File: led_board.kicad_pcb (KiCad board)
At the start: 2 copper layers, 185 x 120 mm, 52 parts, among them J1 Conn_Coaxial, J2 Conn_Coaxial, J3 Conn_Coaxial, J4 Conn_Coaxial, J5 Conn_Coaxial, J6 Conn_Coaxial, J7 Conn_Coaxial, J8 Conn_Coaxial

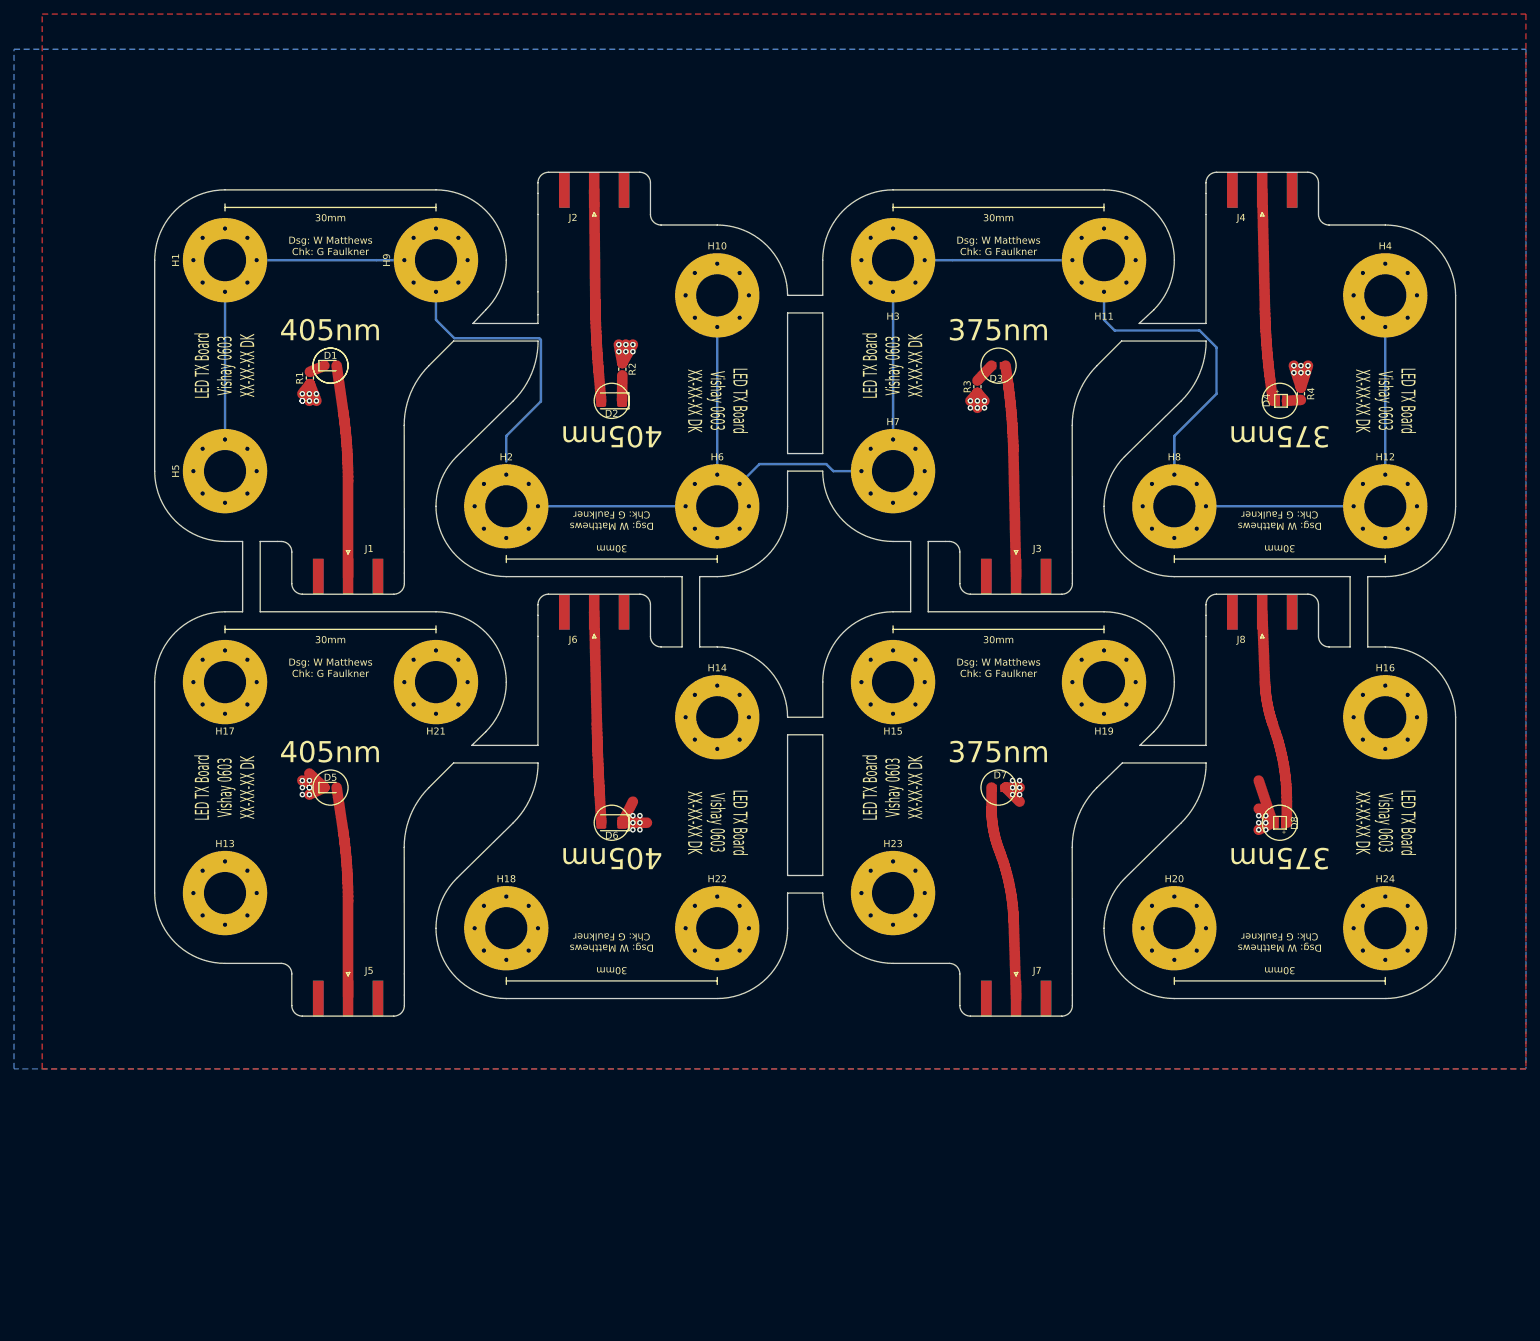
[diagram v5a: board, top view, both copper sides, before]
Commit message: via fencing + mask for all rf traces.
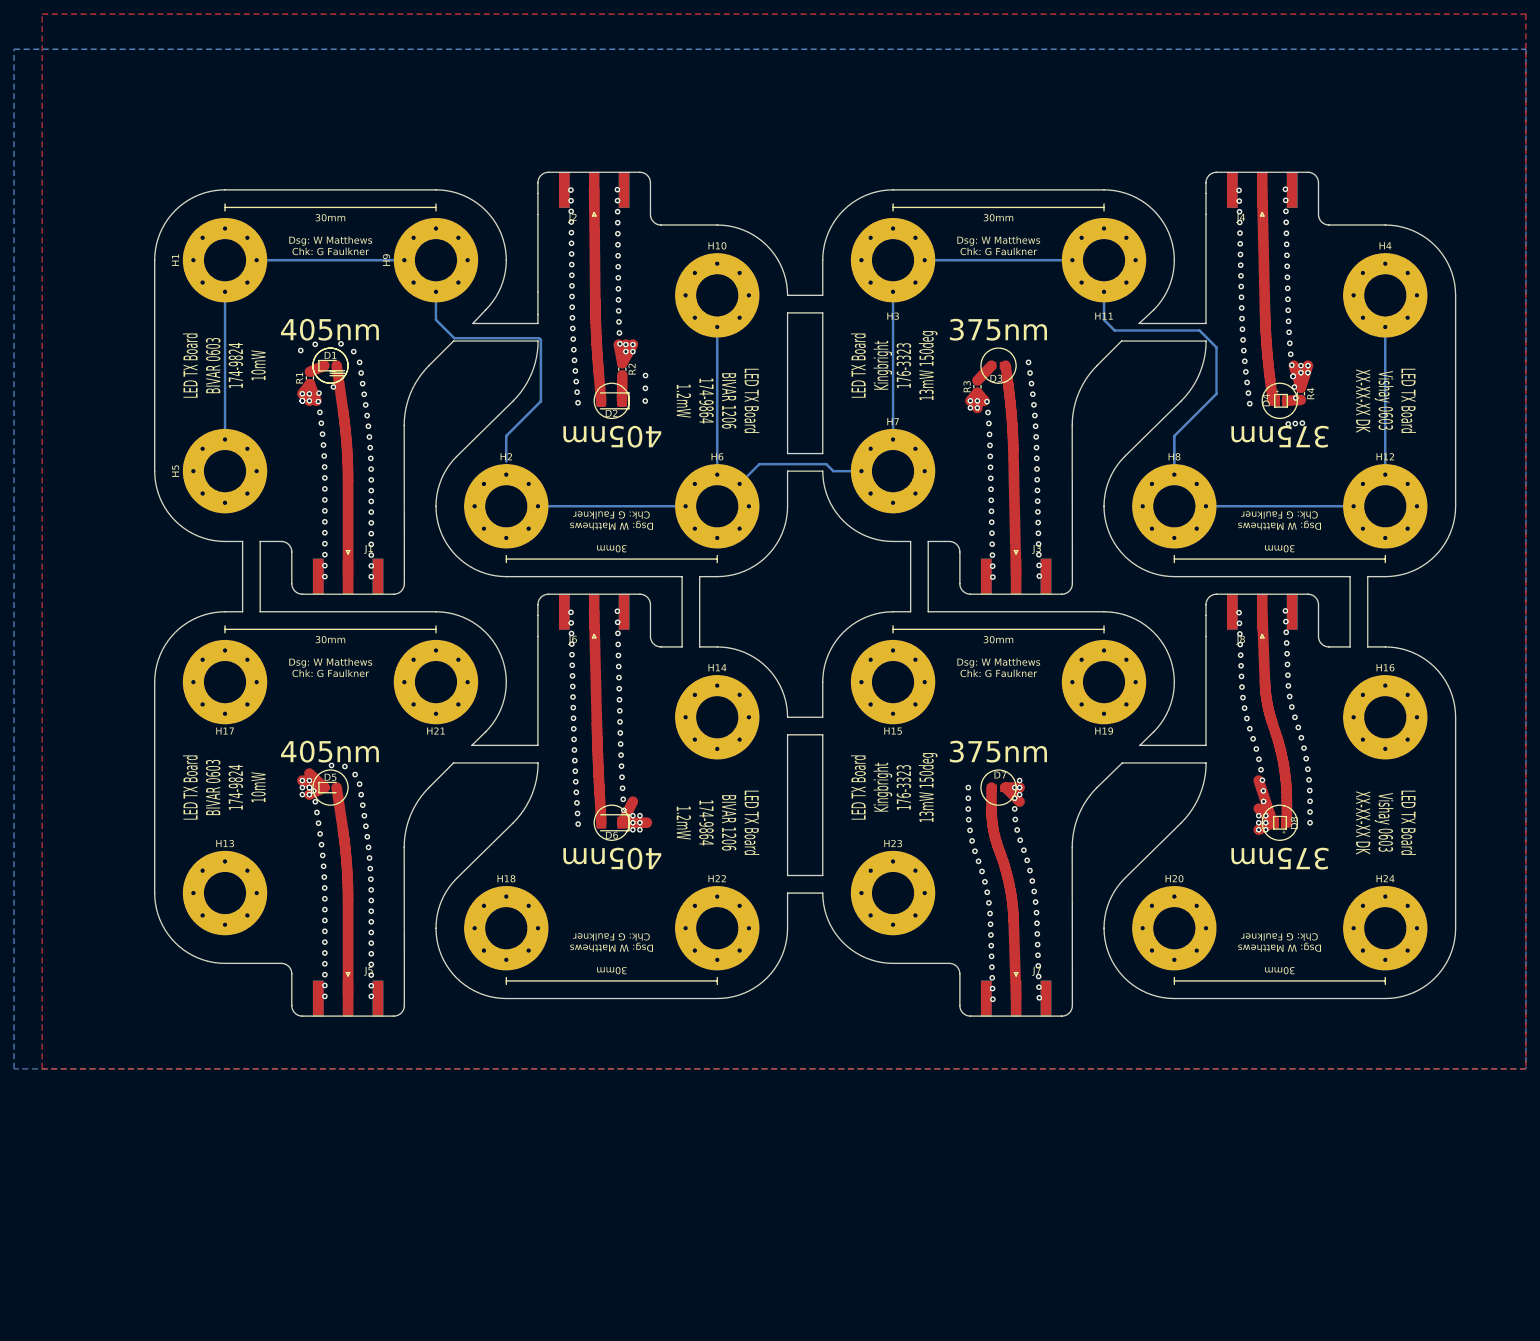
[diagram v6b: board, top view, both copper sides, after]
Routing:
- net Net-(D4-Pad1): vias 0 -> 1
- net GND: vias 51 -> 371
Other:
- board text added: "LED TX Board BIVAR 0603 174-9824 10mW"
- board text added: "LED TX Board BIVAR 1206 174-9864 1.2mW"
- board text added: "LED TX Board Kingbright 176-3323 13mW 150deg"

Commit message: finalised
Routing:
- net GND: track 421.4 -> 489.4 mm, vias 371 -> 373
- net Net-(D4-Pad1): vias 1 -> 0
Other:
- outline, holes or cut-outs redrawn
- board text added: "LED TX Board Vishay 1.6x1.6 133-6267 50mW"
- board text removed: "LED TX Board Vishay 0603 XX-XX-XX DK"

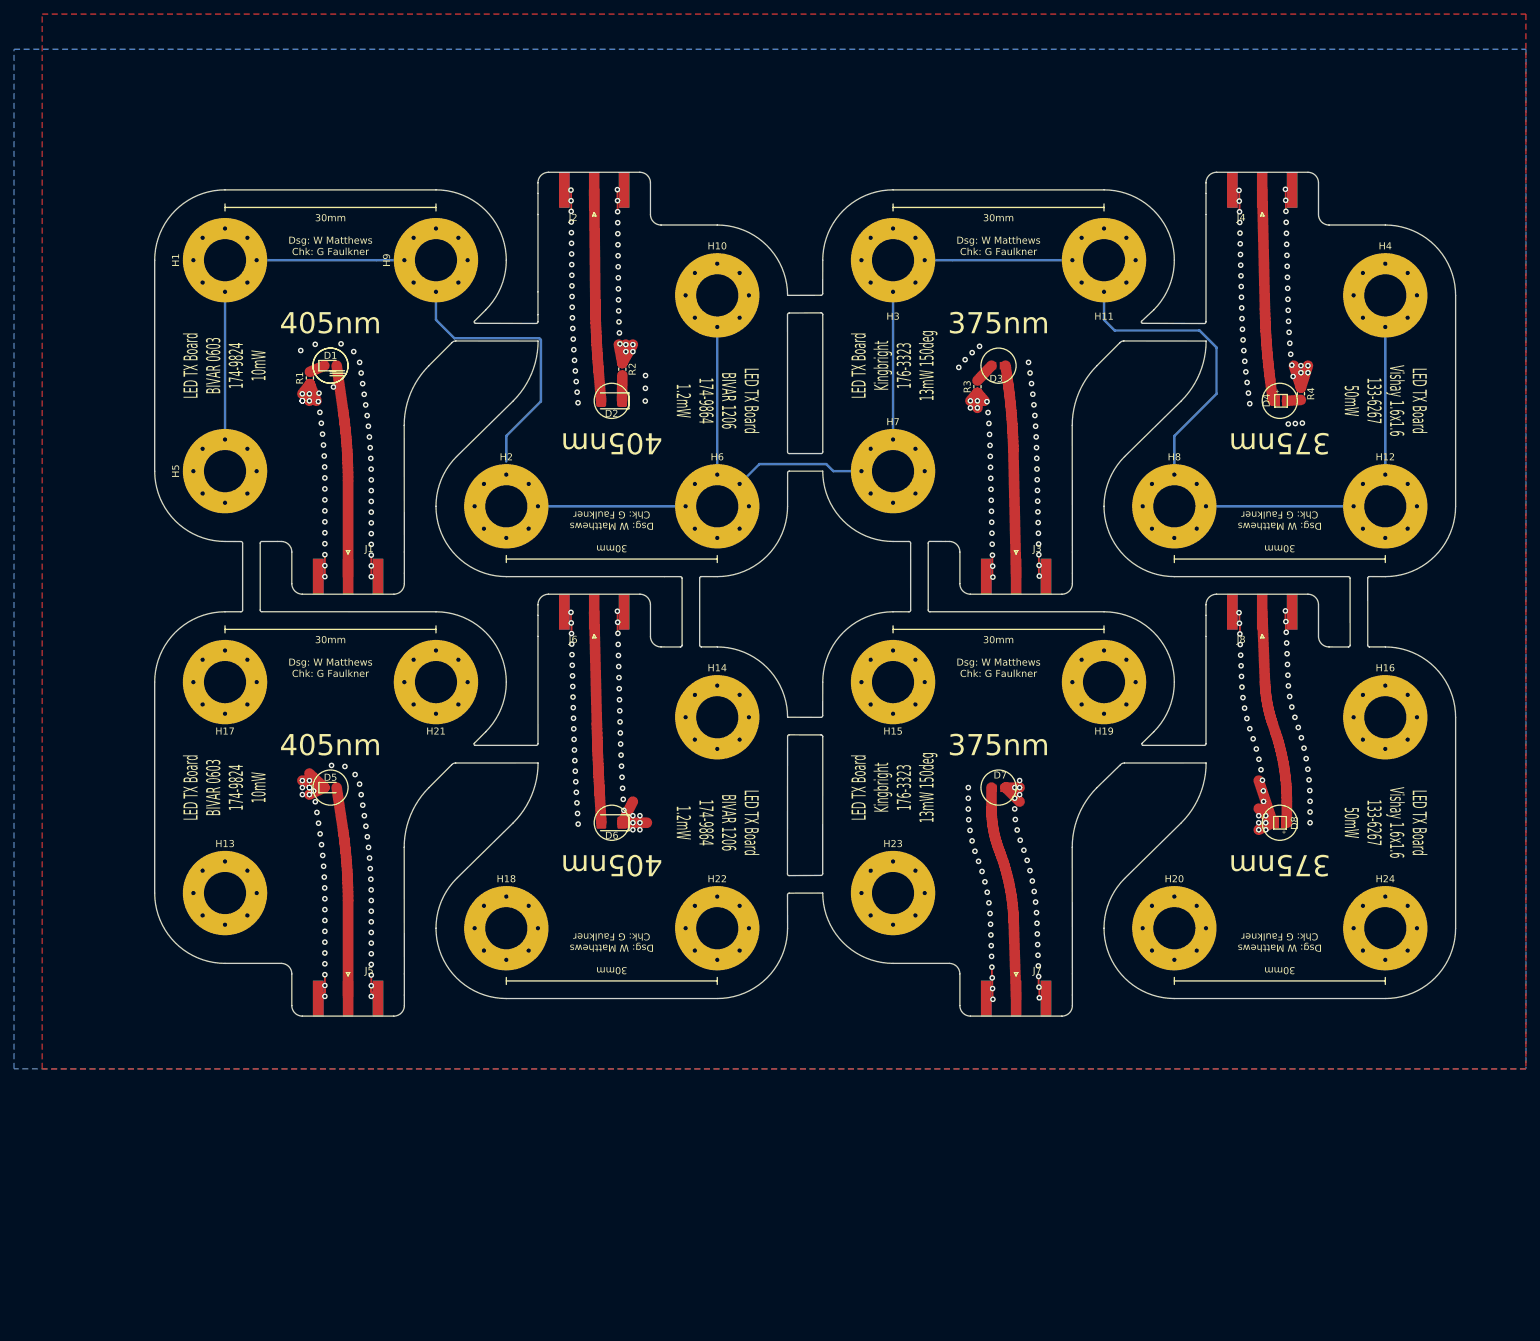
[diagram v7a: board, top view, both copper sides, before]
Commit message: JLC compliant, needs mask and viass
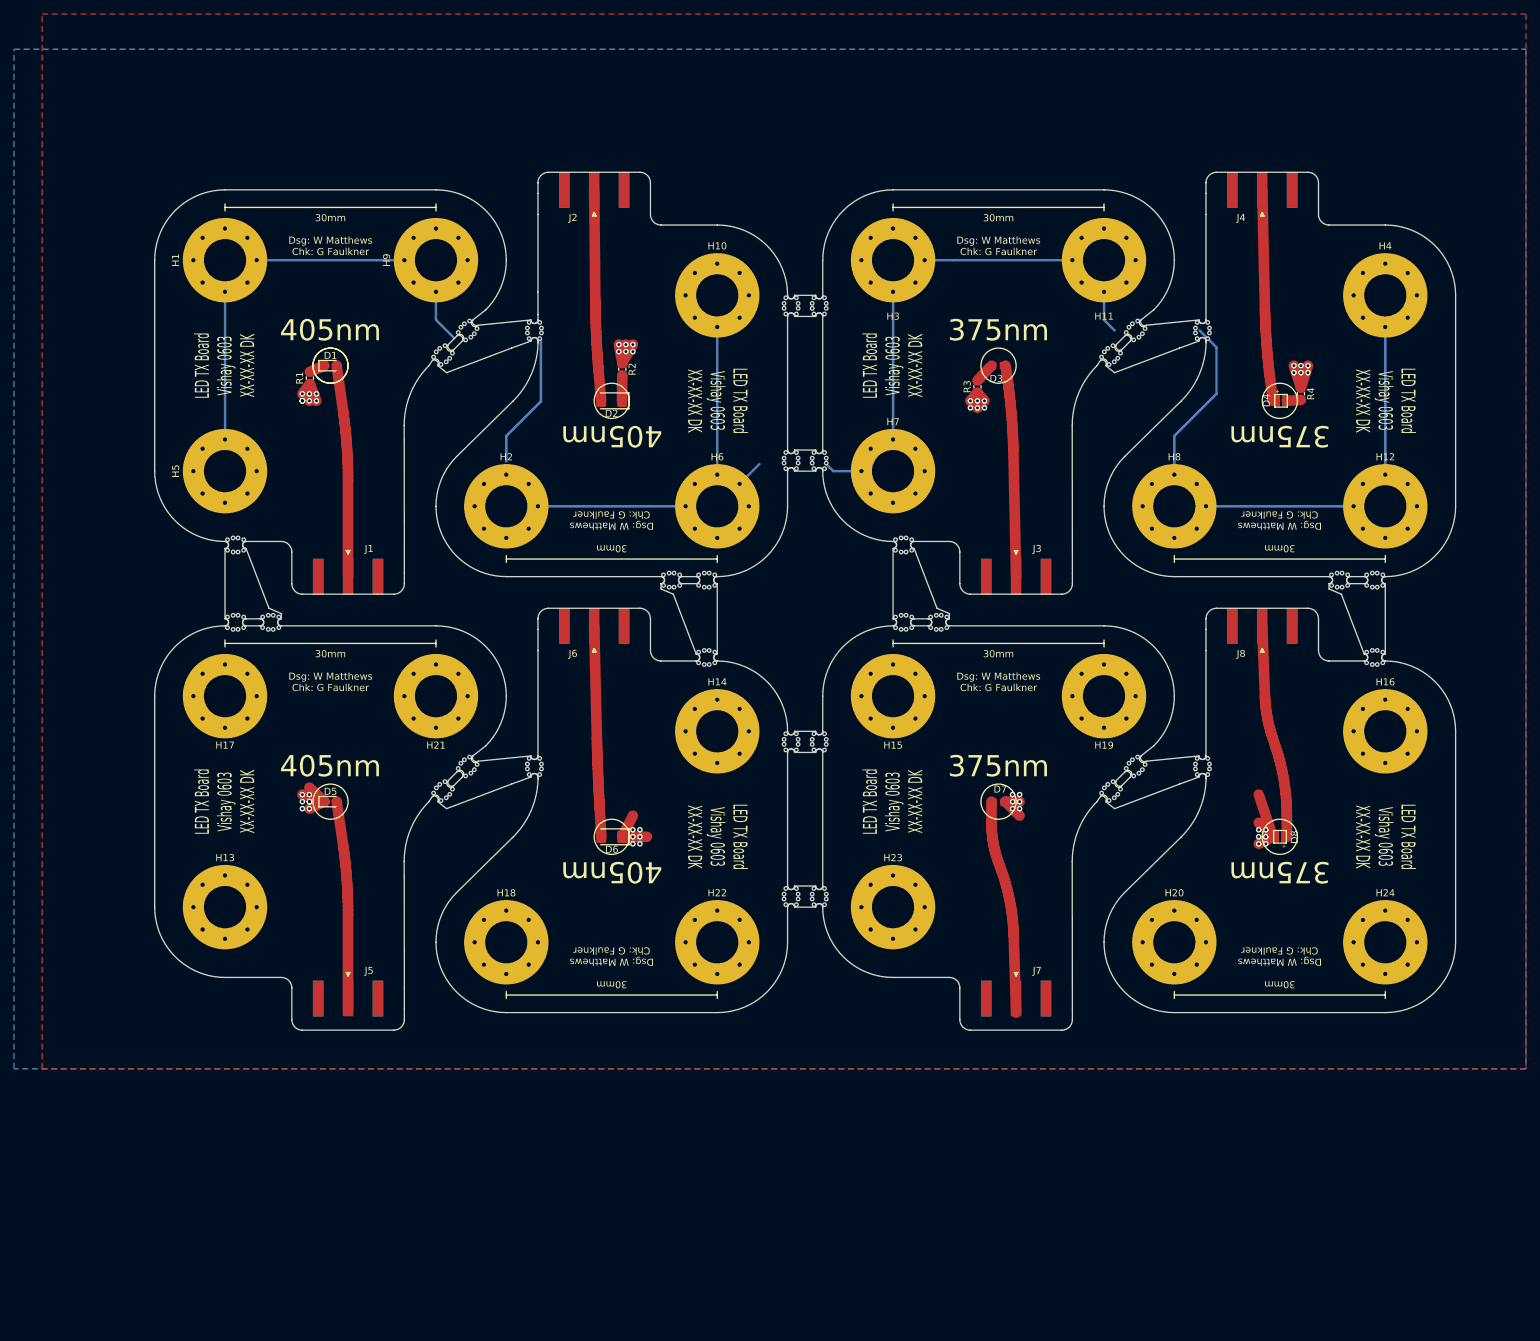
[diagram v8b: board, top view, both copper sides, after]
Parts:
- removed the REF** at (45.0, 110.0)
- removed the REF** at (105.0, 125.0)
- removed the REF** at (140.0, 110.0)
- removed the REF** at (200.0, 125.0)
- added REF**: uv_warn, warnings:uv_warn, B.Cu at (45.0, 112.0)
- added REF**: uv_warn, warnings:uv_warn, B.Cu at (105.0, 127.0)
- added REF**: uv_warn, warnings:uv_warn, B.Cu at (140.0, 112.0)
- added REF**: uv_warn, warnings:uv_warn, B.Cu at (200.0, 127.0)
- added mouse-bite-1mm-slot: VAL**, Panelization:mouse-bite-1mm-slot, F.Cu at (103.5, 85.5)
- added mouse-bite-1mm-slot: VAL**, Panelization:mouse-bite-1mm-slot, F.Cu at (124.5, 68.5)
- added mouse-bite-1mm-slot: VAL**, Panelization:mouse-bite-1mm-slot, F.Cu at (120.5, 68.5)
- added mouse-bite-1mm-slot: VAL**, Panelization:mouse-bite-1mm-slot, F.Cu at (120.5, 46.5)
- added mouse-bite-1mm-slot: VAL**, Panelization:mouse-bite-1mm-slot, F.Cu at (124.5, 46.5)
- added mouse-bite-1mm-slot: VAL**, Panelization:mouse-bite-1mm-slot, F.Cu at (124.5, 130.5)
- added mouse-bite-1mm-slot: VAL**, Panelization:mouse-bite-1mm-slot, F.Cu at (120.5, 130.5)
- added mouse-bite-1mm-slot: VAL**, Panelization:mouse-bite-1mm-slot, F.Cu at (124.5, 108.5)
- added mouse-bite-1mm-slot: VAL**, Panelization:mouse-bite-1mm-slot, F.Cu at (120.5, 108.5)
- added mouse-bite-1mm-slot: VAL**, Panelization:mouse-bite-1mm-slot, F.Cu at (166.0, 53.5)
- added mouse-bite-1mm-slot: VAL**, Panelization:mouse-bite-1mm-slot, F.Cu at (179.0, 50.0)
- added mouse-bite-1mm-slot: VAL**, Panelization:mouse-bite-1mm-slot, F.Cu at (108.5, 96.5)
- added mouse-bite-1mm-slot: VAL**, Panelization:mouse-bite-1mm-slot, F.Cu at (169.5, 50.0)
- added mouse-bite-1mm-slot: VAL**, Panelization:mouse-bite-1mm-slot, F.Cu at (71.0, 53.5)
- added mouse-bite-1mm-slot: VAL**, Panelization:mouse-bite-1mm-slot, F.Cu at (84.0, 50.0)
- added mouse-bite-1mm-slot: VAL**, Panelization:mouse-bite-1mm-slot, F.Cu at (74.5, 50.0)
- added mouse-bite-1mm-slot: VAL**, Panelization:mouse-bite-1mm-slot, F.Cu at (71.0, 115.5)
- added mouse-bite-1mm-slot: VAL**, Panelization:mouse-bite-1mm-slot, F.Cu at (84.0, 112.0)
- added mouse-bite-1mm-slot: VAL**, Panelization:mouse-bite-1mm-slot, F.Cu at (74.5, 112.0)
- added mouse-bite-1mm-slot: VAL**, Panelization:mouse-bite-1mm-slot, F.Cu at (179.0, 112.0)
- added mouse-bite-1mm-slot: VAL**, Panelization:mouse-bite-1mm-slot, F.Cu at (166.0, 115.5)
- added mouse-bite-1mm-slot: VAL**, Panelization:mouse-bite-1mm-slot, F.Cu at (169.5, 112.0)
- added mouse-bite-1mm-slot: VAL**, Panelization:mouse-bite-1mm-slot, F.Cu at (108.5, 85.5)
- added mouse-bite-1mm-slot: VAL**, Panelization:mouse-bite-1mm-slot, F.Cu at (203.5, 96.5)
- added mouse-bite-1mm-slot: VAL**, Panelization:mouse-bite-1mm-slot, F.Cu at (203.5, 85.5)
- added mouse-bite-1mm-slot: VAL**, Panelization:mouse-bite-1mm-slot, F.Cu at (198.5, 85.5)
- added mouse-bite-1mm-slot: VAL**, Panelization:mouse-bite-1mm-slot, F.Cu at (136.5, 80.5)
- added mouse-bite-1mm-slot: VAL**, Panelization:mouse-bite-1mm-slot, F.Cu at (141.5, 91.5)
- added mouse-bite-1mm-slot: VAL**, Panelization:mouse-bite-1mm-slot, F.Cu at (136.5, 91.5)
- added mouse-bite-1mm-slot: VAL**, Panelization:mouse-bite-1mm-slot, F.Cu at (46.5, 91.5)
- added mouse-bite-1mm-slot: VAL**, Panelization:mouse-bite-1mm-slot, F.Cu at (41.5, 80.5)
- added mouse-bite-1mm-slot: VAL**, Panelization:mouse-bite-1mm-slot, F.Cu at (41.5, 91.5)
- moved D5 2.00 mm to (55.0, 117.0)
- moved D6 2.00 mm to (95.0, 122.0)
- moved D7 2.00 mm to (150.2, 115.8)
- moved D8 2.00 mm to (189.2, 122.0)
- moved H13 2.00 mm to (40.0, 132.0)
- moved H14 2.00 mm to (110.0, 107.0)
- moved H15 2.00 mm to (135.0, 102.0)
- moved H16 2.00 mm to (205.0, 107.0)
- moved H17 2.00 mm to (40.0, 102.0)
- moved H18 2.00 mm to (80.0, 137.0)
- moved H19 2.00 mm to (165.0, 102.0)
- moved H20 2.00 mm to (175.0, 137.0)
- moved H21 2.00 mm to (70.0, 102.0)
- moved H22 2.00 mm to (110.0, 137.0)
- moved H23 2.00 mm to (135.0, 132.0)
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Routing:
- net GND: track 489.4 -> 387.7 mm, vias 373 -> 51
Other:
- board size 185 x 120 mm -> 185 x 122 mm
- board text added: "LED TX Board Vishay 0603 XX-XX-XX DK"
- board text removed: "LED TX Board BIVAR 0603 174-9824 10mW"
- board text removed: "LED TX Board BIVAR 1206 174-9864 1.2mW"
- board text removed: "LED TX Board Kingbright 176-3323 13mW 150deg"
- board text removed: "LED TX Board Vishay 1.6x1.6 133-6267 50mW"
